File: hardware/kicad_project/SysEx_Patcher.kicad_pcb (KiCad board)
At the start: 4 copper layers, 172 x 228 mm, 86 parts, among them J1 MIDI_IN, J10 JACK6.35, J2 MIDI_OUT, J3 DC_5V, J4 BAT_PWR, J5 OLED, SW1 prog/MIDI, SW2 SW, SW3 SW, SW4 SW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

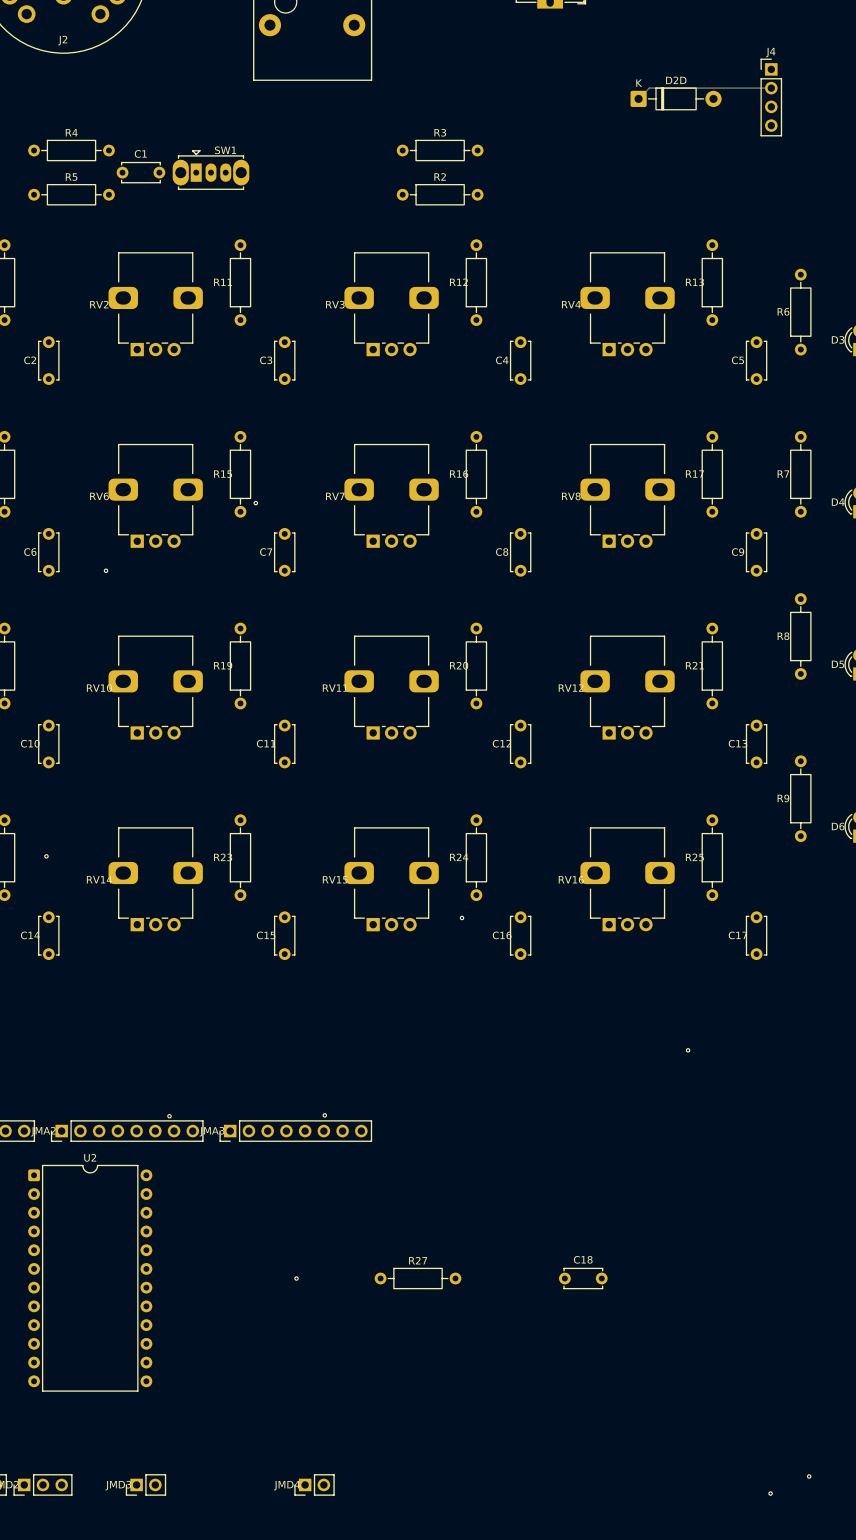
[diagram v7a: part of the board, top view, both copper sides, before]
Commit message: hardware: battery header J4 rotated 90deg + silk pin labels (GND/+5V/GND/VIN)
Relocated J4 below the DC jack so its horizontal row doesn't wall off the OLED
SDA/SCL escape path. Reroute: 0 unconnected, DRC clean; fab Gerbers + previews
regenerated. (drill file copy now includes the no-hyphen .drl)
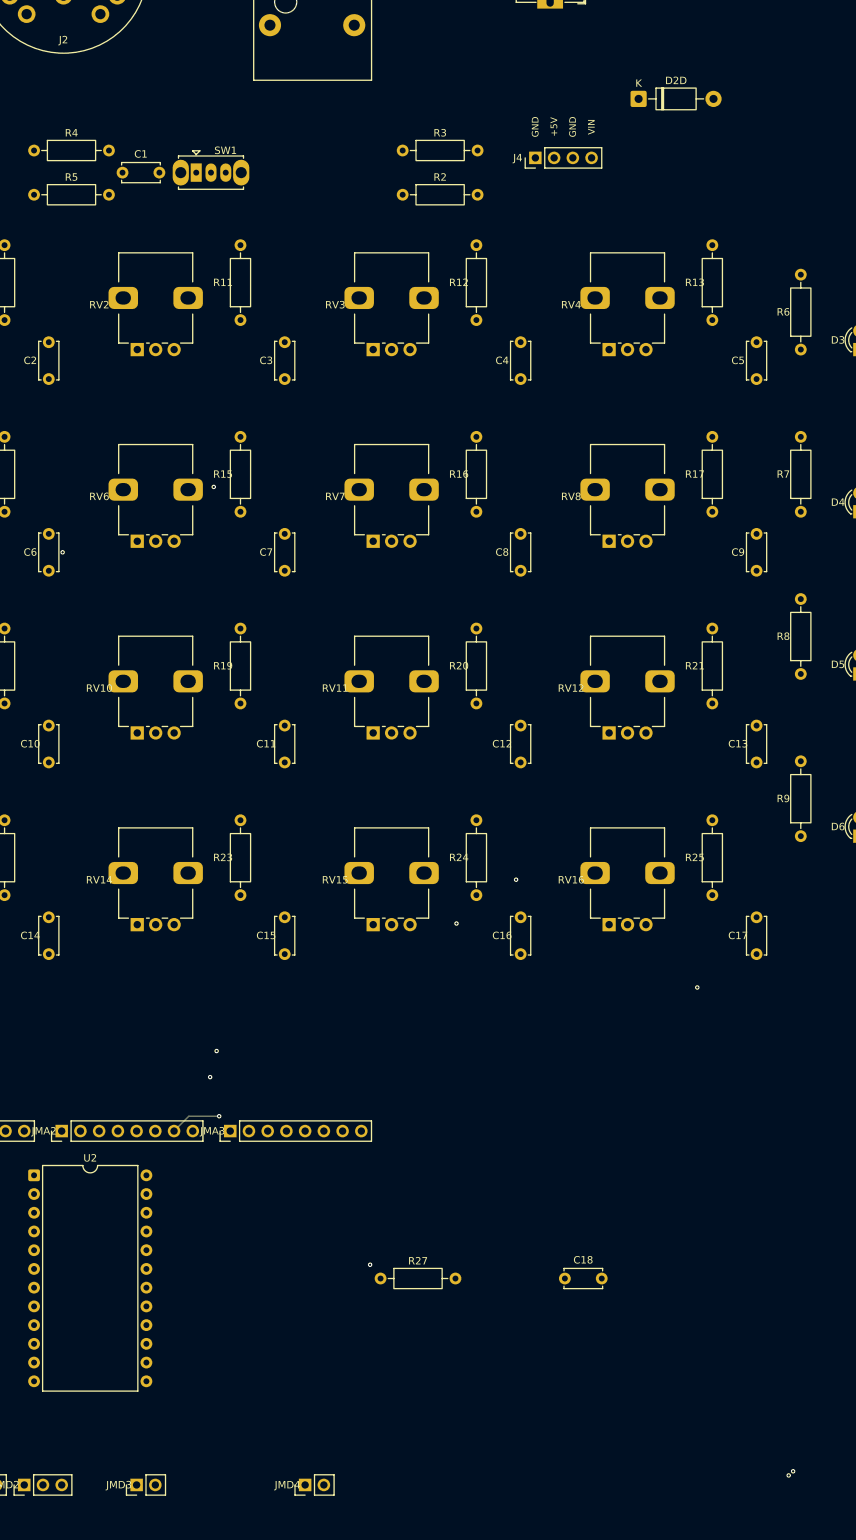
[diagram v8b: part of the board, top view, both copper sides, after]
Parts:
- moved J4 34.2 mm to (116.0, 40.0), turned to 90 degrees
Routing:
- net D11: track 214.7 -> 237.2 mm
- net +5V: track 675.5 -> 656.0 mm
- net VIN_RAW: track 244.9 -> 227.2 mm
- net A4: track 122.6 -> 105.2 mm
- net JACK_W: track 182.9 -> 176.2 mm
- net A12: track 174.8 -> 169.6 mm
- net A8: track 152.3 -> 157.5 mm
- net MUX_CH0: track 147.1 -> 144.3 mm
- net D12: track 255.2 -> 252.5 mm
- net A6: track 76.9 -> 79.3 mm, vias 0 -> 1
- net D20_SDA: track 242.3 -> 241.4 mm
- net D10: track 216.1 -> 216.7 mm
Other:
- board text added: "+5V"
- board text added: "VIN"
